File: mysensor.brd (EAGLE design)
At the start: 48 x 33 mm, 35 parts, among them IC1 LD117AS12TR, IC3 MEGA8-AI

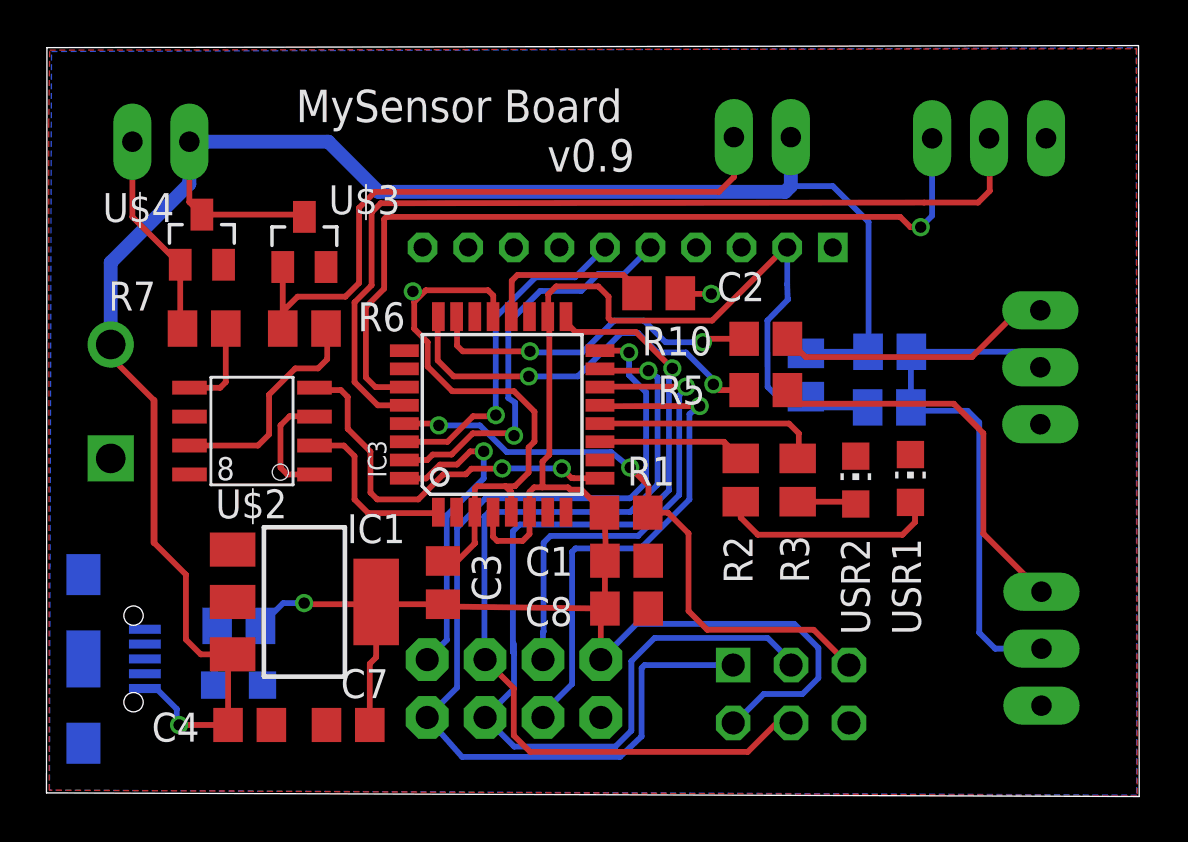
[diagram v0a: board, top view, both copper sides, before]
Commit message: Updates  for rev 1.0
* Moved LDO to left, too close to pin header
* Moved USR1/2 to right for not covered by wifi module
* Removed ground plane under pcb antenna
* Moved GPIO_1 to INT1
* Possible to read battery power by ADC
* Add V+ and GND text to skruvplint

Signed-off-by: Marcus Folkesson <marcus.folkesson@gmail.com>
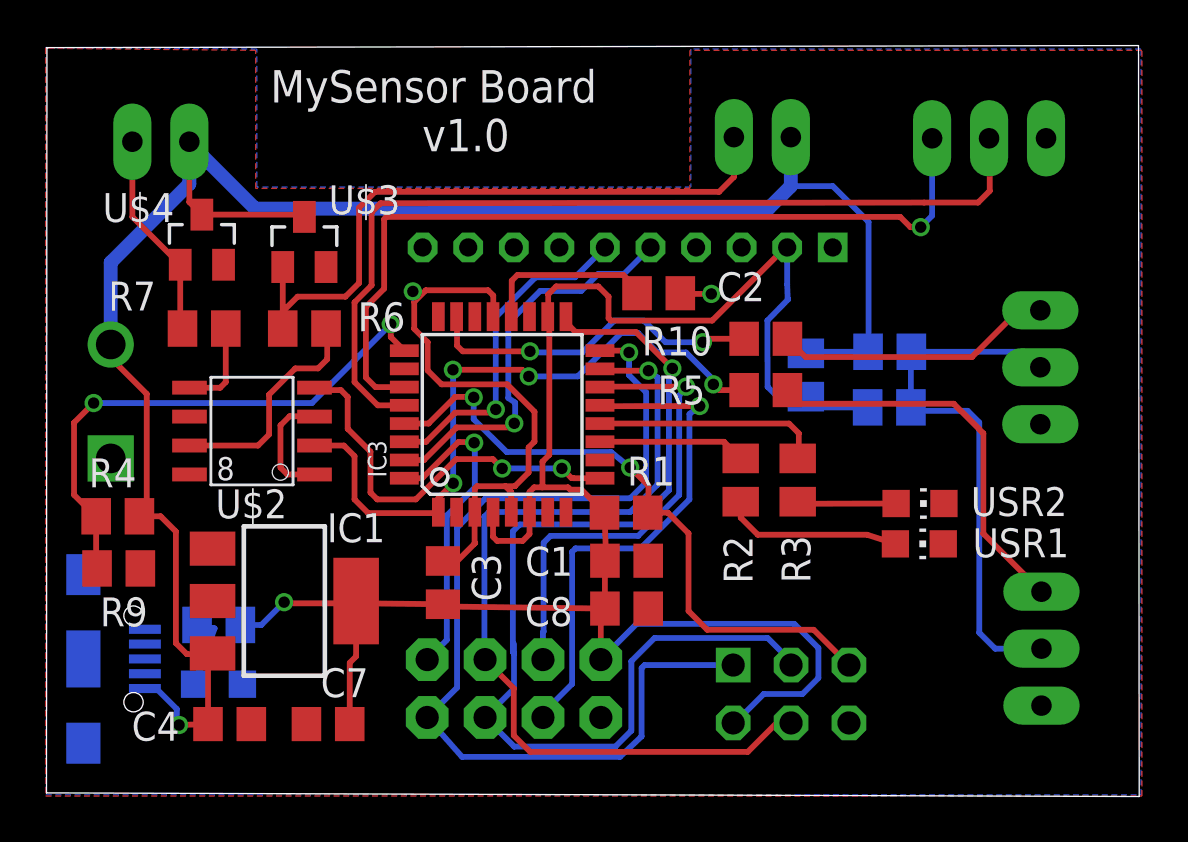
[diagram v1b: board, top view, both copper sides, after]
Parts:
- added R4, R9: 330, rcl:M0805
- moved USR2 3.00 mm to (39.7, 12.8), turned to 270 degrees
- moved USR1 2.90 mm to (39.7, 11.1), turned to 270 degrees
- moved C4 0.88 mm to (9.43, 3.16)
- moved C7 0.88 mm to (13.8, 3.16)
- moved IC1 0.88 mm to (11.8, 8.56)
- moved PWR 0.88 mm to (8.94, 4.91)
- moved R8 0.88 mm to (8.95, 7.51)
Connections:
- new net BATTERY: IC3.25, R4.1, R9.2
- new net GPIO_10: IC3.24
- net +5V: now also R4.2
- net GND: now also R9.1
- net GPIO_1: now also IC3.1; no longer IC3.24
- net GPO_0: now also IC3.2; no longer IC3.1
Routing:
- net BATTERY: track 0.00 -> 23.9 mm, vias 0 -> 2
- net GPIO_1: track 17.6 -> 21.4 mm, vias 2 -> 4
- net N$3: track 9.80 -> 7.86 mm
- net N$4: track 2.59 -> 4.36 mm
- net RESET: track 26.6 -> 28.1 mm
- net +3V3: track 87.1 -> 88.0 mm
- net N$2: track 2.65 -> 3.39 mm
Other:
- board text added: "GND"
- board text added: "V+"
- board text added: "v1.0"
- board text removed: "v0.9"

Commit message: Unknown changes
Signed-off-by: Marcus Folkesson <marcus.folkesson@gmail.com>
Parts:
- added R11: 4.7k, rcl:M0805
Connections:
- new net N$7: R11.1, U$1.P$3, U$1.P$4
- new net NO: IC3.2
- net +3V3: now also R11.2
- net GPO_0: now also IC3.9; no longer IC3.2
- net GPO_1: now also IC3.10; no longer IC3.9
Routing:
- net N$7: track 0.00 -> 17.6 mm, vias 0 -> 1
- net GPO_0: track 7.74 -> 15.2 mm, vias 0 -> 2
- net +3V3: track 88.0 -> 93.0 mm, vias 1 -> 2
- net GND: track 31.1 -> 27.7 mm
- net GPIO_1: track 21.4 -> 24.6 mm
- net RESET: track 28.1 -> 29.3 mm
